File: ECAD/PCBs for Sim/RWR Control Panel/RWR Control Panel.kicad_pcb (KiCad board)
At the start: 2 copper layers, 93 x 40.6 mm, 43 parts, among them J1 PWR, J2 BUS IN, J3 BUS OUT, J4 PGM SEL, J5 RPOT1, J6 RPOT2, J7 5POS, P1 Digital, P2 Analog, P3 CONN_01X01, P4 CONN_01X01, P5 CONN_01X01, P6 CONN_01X01, SW1 SW_Push, SW2 SW_Push, SW3 SW_Push, SW4 SW_Push, SW5 SW_Push, U1 MAX487EESA, U2 STP16CPC26

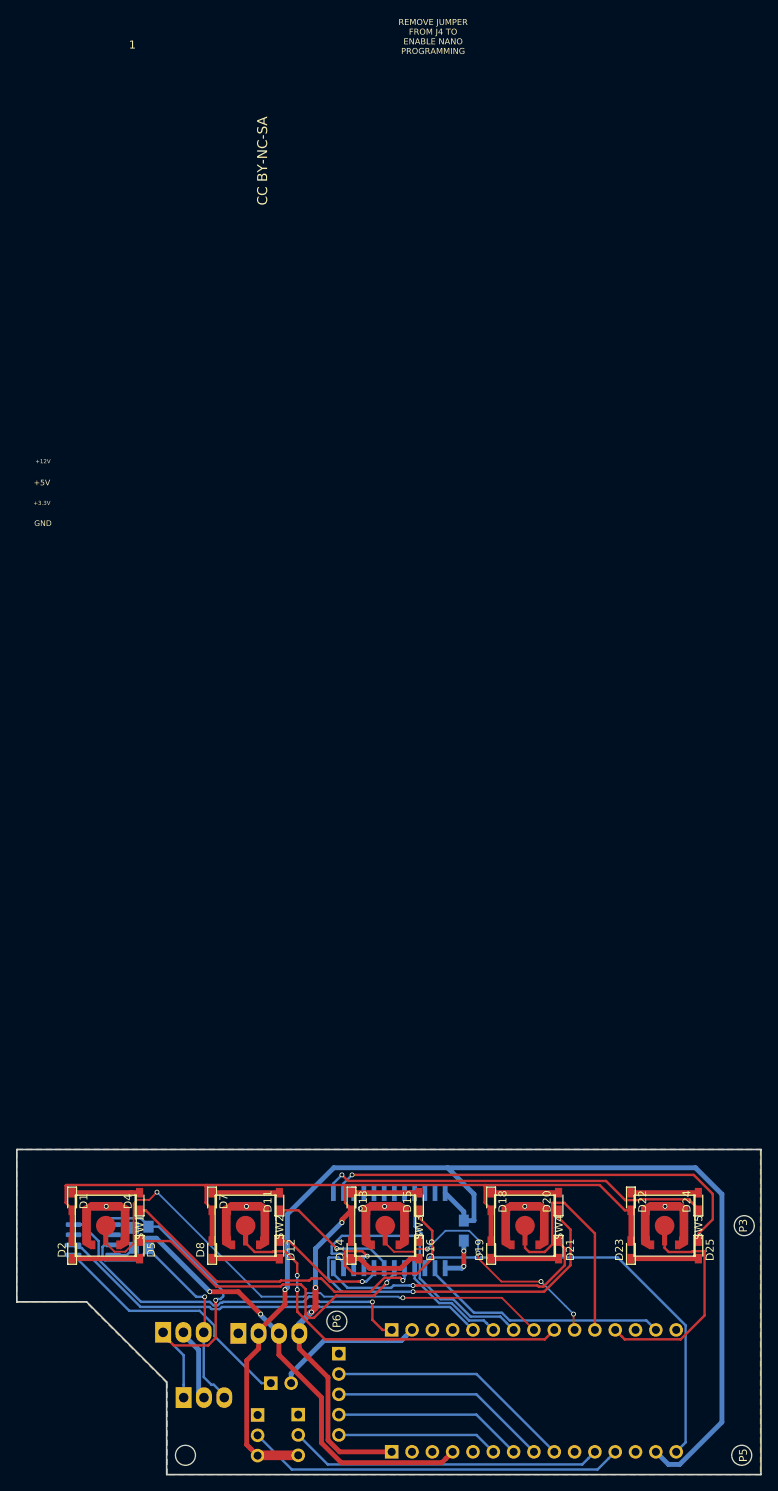
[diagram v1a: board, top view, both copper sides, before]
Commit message: rerouted RWR panel
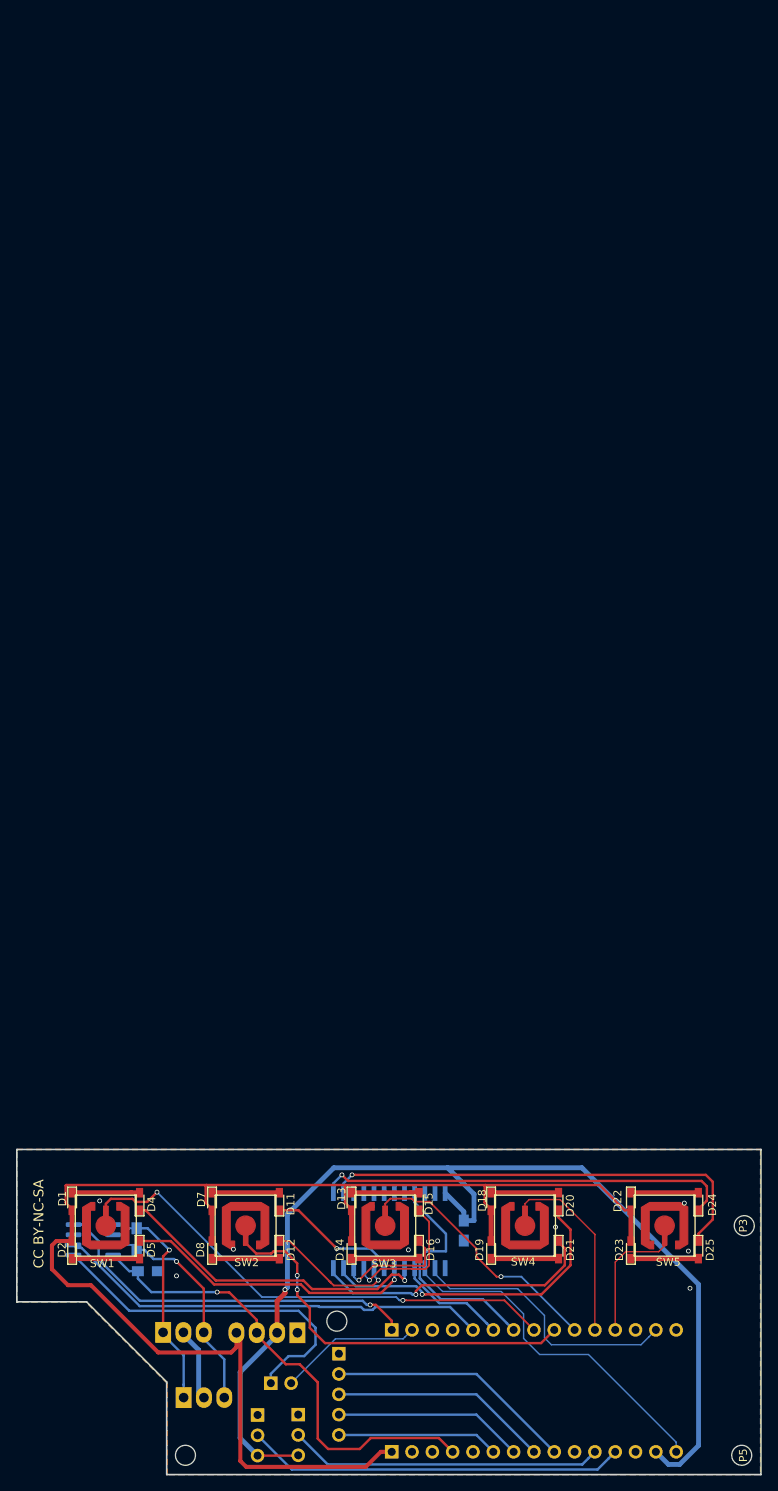
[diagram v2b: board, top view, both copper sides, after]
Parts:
- moved J1 7.39 mm to (135.9, 104.6), turned to 180 degrees
- moved C1 4.52 mm to (117.3, 96.9), turned to 0 degrees
- moved R1 1.48 mm to (115.9, 92.9)
- turned SW1 to 90 degrees
- turned SW3 to 90 degrees
- turned SW4 to 90 degrees
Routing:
- net GND: track 95.9 -> 10.5 mm, vias 8 -> 9
- net +12V: track 147.4 -> 176.6 mm, vias 3 -> 0
- net Net-(J2-Pad1): track 45.0 -> 28.6 mm
- net /RX_ENABLE: track 32.1 -> 44.4 mm
- net /9(**): track 28.9 -> 16.8 mm
- net +3V3: track 149.3 -> 139.3 mm
- net /13(SCK): track 53.4 -> 43.8 mm
- net Net-(D15-Pad1): track 25.7 -> 17.5 mm
- net /8: track 30.9 -> 24.2 mm
- net Net-(D20-Pad1): track 45.3 -> 39.3 mm
- net /5(**): track 69.6 -> 64.3 mm
- net Net-(D5-Pad1): track 41.0 -> 36.7 mm
- net Net-(J2-Pad3): track 32.8 -> 28.4 mm
- net /4: track 25.5 -> 29.5 mm
- net /11(**/MOSI): track 31.2 -> 34.4 mm
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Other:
- net class control: trace_width 0.2286 -> 0.1778
- net class pwr12v: trace_width 0.762 -> 0.508
- board text removed: "+12V"
- board text removed: "+3.3V"
- board text removed: "+5V"
- board text removed: "1"
- board text removed: "GND"

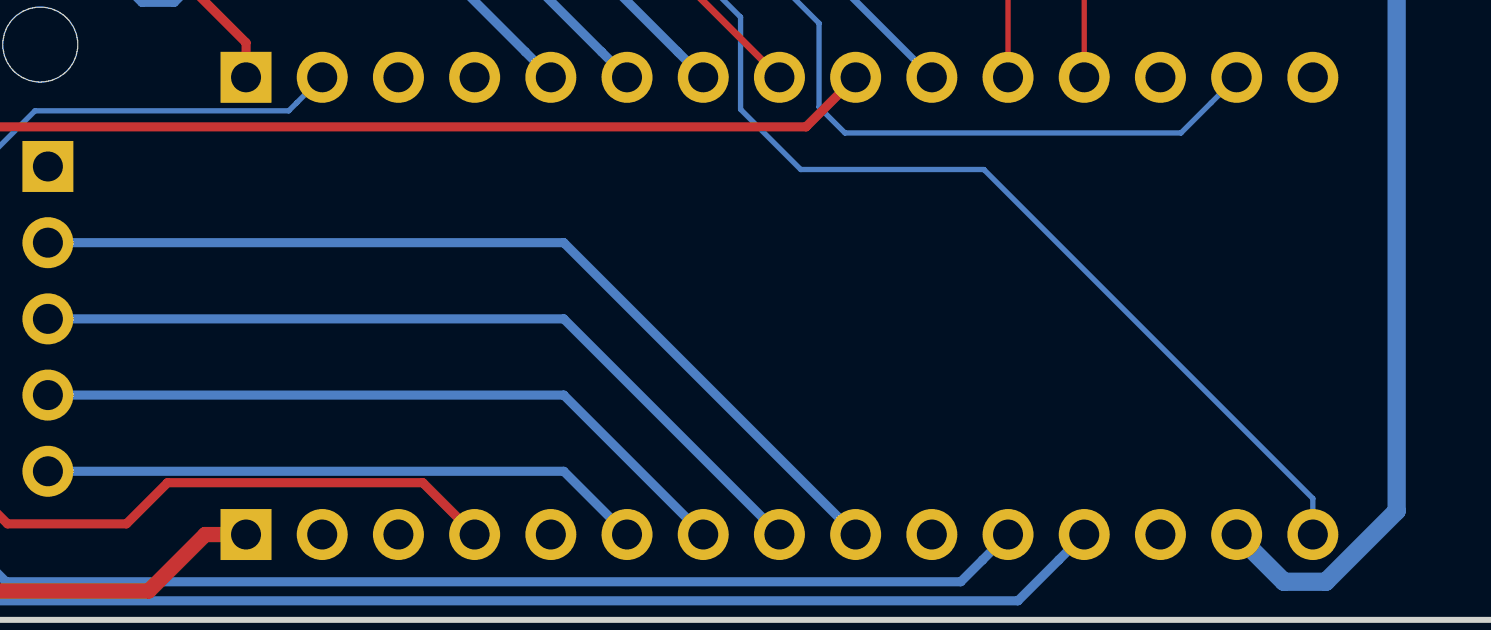
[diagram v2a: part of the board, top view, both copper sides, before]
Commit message: RWR Control Panel Manufacturing Files
Added OH branding to the PCB. Created the gerbers, bom, pick and place data and the step MCAD file.
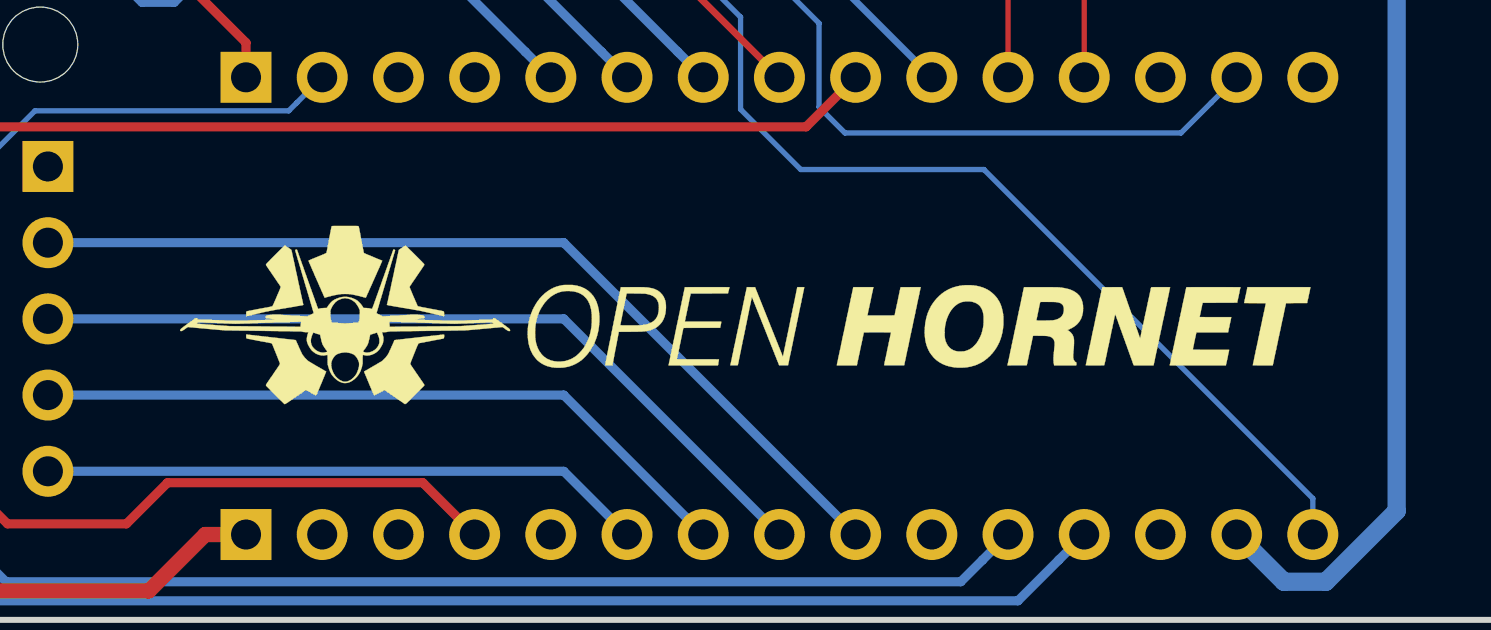
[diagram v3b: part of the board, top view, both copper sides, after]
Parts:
- added G***: LOGO, KiCAD Libraries:OH_LOGO_37.7mm_5.9mm, F.Cu at (164.4, 112.2)
